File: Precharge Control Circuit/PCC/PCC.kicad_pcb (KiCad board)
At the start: 2 copper layers, 190.6 x 151.7 mm, 128 parts, among them J1 Conn_01x04_Socket, J10 AMP BYP, J11 AMP BYP, J2 874271202, J3 462070206, J4 Conn_02x14_Counter_Clockwise, J5 IMD, J6 Thermistor Expansion, J7 RTM, J8 BMS, J9 EnergyMeter, K1 Relay_SPDT, K2 PCN-112D3MHZ_000, Q1 IRLZ44N, Q2 IRLZ44N, U1 SN65HVD230, U2 4N35, U3 4N35, U7 TLV2372IP, U8 LM1117T-5.0

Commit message: Fixed Copper Zones on Resistor Divider, Fixed Mounting Holes and Placement, adjusted traces
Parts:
- added H1: MountingHole_Pad, MountingHole:MountingHole_3.2mm_M3_DIN965_Pad_TopBottom, F.Cu at (233.5, 21.2)
- added H2: MountingHole_Pad, MountingHole:MountingHole_3.2mm_M3_DIN965_Pad_TopBottom, F.Cu at (233.5, 158.8)
- added H3: MountingHole_Pad, MountingHole:MountingHole_3.2mm_M3_DIN965_Pad_TopBottom, F.Cu at (57.0, 20.7)
- added H4: MountingHole_Pad, MountingHole:MountingHole_3.2mm_M3_DIN965_Pad_TopBottom, F.Cu at (77.4, 160.5)
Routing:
- net +12 ISO: track 117.7 -> 123.5 mm, vias 8 -> 10
- net B+_in: track 124.4 -> 122.6 mm
- net /FusedTS+4: track 8.54 -> 6.90 mm
- net /FusedTS-2: track 15.9 -> 14.6 mm
- net /FusedTS+1: track 10.1 -> 8.96 mm
- net Net-(F5-Pad2): track 16.3 -> 15.5 mm
- net TS-: track 174.0 -> 173.4 mm
- added copper zone on B.Cu, net Net-(R1-Pad2)
- added copper zone on B.Cu, net Net-(R2-Pad2)
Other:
- outline, holes or cut-outs redrawn

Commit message: Acid Traps
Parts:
- moved R57 8.51 mm to (155.1, 81.2), turned to 180 degrees
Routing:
- net TS+: track 294.6 -> 308.9 mm
- net GLV+: track 256.7 -> 267.1 mm
- net Net-(R57-Pad2): track 11.4 -> 2.92 mm
- net GND ISO: track 42.9 -> 44.9 mm, vias 0 -> 1
- net Net-(F11-Pad2): track 16.6 -> 15.4 mm
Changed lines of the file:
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@@
 	(footprint "Resistor_SMD:R_0805_2012Metric"
 		(layer "B.Cu")
-		(at 159.004 73.66 -90)
+		(at 155.0875 81.21525 180)
 		(descr "Resistor SMD 0805 (2012 Metric), square (rectangular) end terminal, IPC-7351 nominal, (Body size source: IPC-SM-782 page 72, https://www.pcb-3d.com/wordpress/wp-content/uploads/ipc-sm-782a_amendment_1_and_2.pdf), generated with kicad-footprint-generator")
 		(tags "resistor")
 		(property "Reference" "R57"
-			(at 0 1.65 90)
+			(at 0 1.65 0)
 			(layer "B.SilkS")
 			(effects
@@
 		)
 		(property "Value" "510K"
-			(at 0 -1.65 90)
+			(at 0 -1.65 0)
 			(layer "B.Fab")
 			(effects
@@
 		)
 		(property "Datasheet" "https://www.digikey.com/en/products/detail/panasonic-electronic-components/ERJ-6GEYJ514V/83144"
-			(at 0 0 90)
+			(at 0 0 0)
 			(layer "B.Fab")
 			(hide yes)
@@
 		)
 		(property "Description" "Resistor, US symbol"
-			(at 0 0 90)
+			(at 0 0 0)
 			(layer "B.Fab")
 			(hide yes)
@@
 		)
 		(property "MFG" "Panasonic Electronic Components "
-			(at 0 0 270)
+			(at 0 0 180)
 			(unlocked yes)
 			(layer "B.Fab")
@@
 		)
 		(property "MPN" "ERJ-6GEYJ514V "
-			(at 0 0 270)
+			(at 0 0 180)
 			(unlocked yes)
 			(layer "B.Fab")
@@
 		)
 		(fp_text user "${REFERENCE}"
-			(at 0 0 90)
+			(at 0 0 0)
 			(layer "B.Fab")
 			(effects
@@
 		)
 		(pad "1" smd roundrect
-			(at -0.9125 0 270)
+			(at -0.9125 0 180)
 			(size 1.025 1.4)
 			(layers "B.Cu" "B.Mask" "B.Paste")
@@
 		)
 		(pad "2" smd roundrect
-			(at 0.9125 0 270)
+			(at 0.9125 0 180)
 			(size 1.025 1.4)
 			(layers "B.Cu" "B.Mask" "B.Paste")
@@
 		(net 7)
 	)
+	(via
+		(at 123.698 67.818)
+		(size 0.6)
+		(drill 0.3)
+		(layers "F.Cu" "B.Cu")
+		(net 8)
+	)
+	(segment
+		(start 124.559288 81.21525)
+		(end 124.302269 81.472269)
+		(width 0.7)
+		(layer "B.Cu")
+		(net 8)
+	)
 	(segment
 		(start 122.425 83.37675)
@@
 	)
 	(segment
-		(start 124.559288 81.21525)
+		(start 124.302269 81.472269)
 		(end 122.425 83.349538)
 		(width 0.7)
@@
 	)
 	(segment
+		(start 124.302269 80.304981)
+		(end 123.698 79.700712)
+		(width 0.7)
+		(layer "B.Cu")
+		(net 8)
+	)
+	(segment
 		(start 148.475 28.59)
 		(end 133.41 28.59)
@@
 	)
 	(segment
+		(start 124.302269 81.472269)
+		(end 124.302269 80.304981)
+		(width 0.7)
+		(layer "B.Cu")
+		(net 8)
+	)
+	(segment
 		(start 132.4635 81.21525)
 		(end 125.212538 81.21525)
@@
 	)
 	(segment
-		(start 158.75 71.882)
-		(end 158.75 62.75)
+		(start 167.879 71.879)
+		(end 171.876995 71.879)
 		(width 2)
 		(layer "B.Cu")
@@
 	)
 	(segment
+		(start 156 65.5)
+		(end 158.75 62.75)
+		(width 0.5)
+		(layer "B.Cu")
+		(net 41)
+	)
+	(segment
 		(start 200.475747 164.259253)
 		(end 213.36 151.375)
@@
 	)
 	(segment
-		(start 171.873995 71.882)
-		(end 158.75 71.882)
-		(width 2)
-		(layer "B.Cu")
-		(net 41)
-	)
-	(segment
 		(start 213.36 75.955)
 		(end 209.287 71.882)
@@
 	)
 	(segment
+		(start 156 81.21525)
+		(end 156 65.5)
+		(width 0.5)
+		(layer "B.Cu")
+		(net 41)
+	)
+	(segment
+		(start 158.75 62.75)
+		(end 167.879 71.879)
+		(width 2)
+		(layer "B.Cu")
+		(net 41)
+	)
+	(segment
 		(start 111.25 145.2125)
 		(end 115.5375 149.5)
@@
 	)
 	(segment
-		(start 61.45 124.79)
+		(start 63.87 124.79)
 		(end 65.000502 124.79)
 		(width 2)
@@
 	)
 	(segment
+		(start 64.253304 85.346699)
+		(end 67.44 85.346699)
+		(width 2)
+		(layer "B.Cu")
+		(net 48)
+	)
+	(segment
 		(start 68.901 128.690498)
 		(end 68.901 134.189)
@@
 	)
 	(segment
-		(start 68.901 134.189)
+		(start 61.45 124.79)
+		(end 63.87 124.79)
+		(width 2)
+		(layer "B.Cu")
+		(net 48)
+	)
+	(segment
+		(start 66.355 136.735)
 		(end 64.55 138.54)
 		(width 2)
@@
 	)
 	(segment
+		(start 67.44 85.346699)
+		(end 67.44 82.160004)
+		(width 2)
+		(layer "B.Cu")
+		(net 48)
+	)
+	(segment
+		(start 65.905251 139.694749)
+		(end 65.905251 137.184749)
+		(width 2)
+		(layer "B.Cu")
+		(net 48)
+	)
+	(segment
+		(start 68.901 134.189)
+		(end 66.355 136.735)
+		(width 2)
+		(layer "B.Cu")
+		(net 48)
+	)
+	(segment
+		(start 66.155251 139.944749)
+		(end 65.905251 139.694749)
+		(width 2)
+		(layer "B.Cu")
+		(net 48)
+	)
+	(segment
 		(start 60.399 102.04205)
 		(end 60.399 109.489)
@@
 	)
 	(segment
-		(start 64.253304 85.346699)
+		(start 67.44 82.160004)
+		(end 67.820002 81.780002)
+		(width 2)
+		(layer "B.Cu")
+		(net 48)
+	)
+	(segment
+		(start 67.44 85.346699)
 		(end 71.344183 85.346699)
 		(width 2)
@@
 	)
 	(segment
+		(start 64.38 121.86)
+		(end 61.45 124.79)
+		(width 2)
+		(layer "B.Cu")
+		(net 48)
+	)
+	(segment
+		(start 67.820002 81.780002)
+		(end 61.300001 88.300002)
+		(width 2)
+		(layer "B.Cu")
+		(net 48)
+	)
+	(segment
 		(start 71.344183 85.346699)
 		(end 72.962301 86.964817)
@@
 	)
 	(segment
+		(start 65.905251 137.184749)
+		(end 66.355 136.735)
+		(width 2)
+		(layer "B.Cu")
+		(net 48)
+	)
+	(segment
 		(start 61.300001 74.300002)
 		(end 64.253304 71.346699)
@@
 	)
 	(segment
+		(start 63.87 122.37)
+		(end 64.38 121.86)
+		(width 2)
+		(layer "B.Cu")
+		(net 48)
+	)
+	(segment
 		(start 68.901 114.440498)
 		(end 68.901 117.339)
@@
 	(segment
 		(start 68.901 117.339)
-		(end 61.45 124.79)
+		(end 64.38 121.86)
 		(width 2)
 		(layer "B.Cu")
@@
 	)
 	(segment
-		(start 64.750502 138.54)
+		(start 66.155251 139.944749)
 		(end 68.651 142.440498)
 		(width 2)
@@
 	)
 	(segment
+		(start 64.750502 138.54)
+		(end 66.155251 139.944749)
+		(width 2)
+		(layer "B.Cu")
+		(net 48)
+	)
+	(segment
 		(start 72.962301 86.964817)
 		(end 72.962301 89.478749)
@@
 	)
 	(segment
+		(start 63.87 124.79)
+		(end 63.87 122.37)
+		(width 2)
+		(layer "B.Cu")
+		(net 48)
+	)
+	(segment
 		(start 72.962301 89.478749)
 		(end 60.399 102.04205)
@@
 	(segment
 		(start 72.962301 76.637702)
-		(end 61.300001 88.300002)
+		(end 67.820002 81.780002)
 		(width 2)
 		(layer "B.Cu")
@@
 	)
 	(segment
-		(start 154.49675 81.21525)
-		(end 159.004 76.708)
-		(width 0.2)
-		(layer "B.Cu")
-		(net 83)
-	)
-	(segment
-		(start 159.004 76.708)
-		(end 159.004 74.5725)
-		(width 0.2)
-		(layer "B.Cu")
-		(net 83)
-	)
-	(segment
 		(start 102.445 44.25)
 		(end 101.195253 43.000253)
@@
 	)
 	(segment
-		(start 197.9515 100.33)
-		(end 199.7295 102.108)
-		(width 0.7)
-		(layer "B.Cu")
-		(net 109)
-	)
-	(segment
-		(start 189.475 100.33)
-		(end 197.9515 100.33)
+		(start 201.3965 102.108)
+		(end 191.253 102.108)
 		(width 0.7)
 		(layer "B.Cu")
@@
 	)
 	(segment
-		(start 199.7295 102.108)
-		(end 201.3965 102.108)
+		(start 191.253 102.108)
+		(end 189.475 100.33)
 		(width 0.7)
 		(layer "B.Cu")
@@
 	)
 	(segment
-		(start 195.624 88.265)
-		(end 198.037 85.852)
+		(start 193.158 85.852)
+		(end 190.745 88.265)
 		(width 0.7)
 		(layer "B.Cu")
@@
 	)
 	(segment
-		(start 198.037 85.852)
-		(end 199.4915 85.852)
+		(start 199.4915 85.852)
+		(end 193.158 85.852)
 		(width 0.7)
 		(layer "B.Cu")
@@
 	)
 	(segment
-		(start 190.745 88.265)
-		(end 195.624 88.265)
-		(width 0.7)
-		(layer "B.Cu")
-		(net 110)
-	)
-	(segment
-		(start 230.759 108.0515)
-		(end 230.759 106.724)
-		(width 0.7)
-		(layer "B.Cu")
-		(net 111)
-	)
-	(segment
-		(start 230.759 106.724)
-		(end 229.235 105.2)
-		(width 0.7)
-		(layer "B.Cu")
-		(net 111)
-	)
-	(segment
-		(start 229.235 105.2)
+		(start 230.759 94.479)
 		(end 229.235 92.955)
 		(width 0.7)
@@
 	)
 	(segment
-		(start 213.36 92.955)
-		(end 220.546 92.955)
+		(start 230.759 108.0515)
+		(end 230.759 94.479)
 		(width 0.7)
 		(layer "B.Cu")
-		(net 112)
+		(net 111)
 	)
 	(segment
-		(start 220.546 92.955)
-		(end 225.806 98.215)
+		(start 220.5825 100.1775)
+		(end 213.36 92.955)
 		(width 0.7)
 		(layer "B.Cu")
@@
 	)
 	(segment
-		(start 225.806 98.215)
-		(end 225.806 100.1775)
+		(start 225.806 100.1775)
+		(end 220.5825 100.1775)
 		(width 0.7)
 		(layer "B.Cu")

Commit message: PCC rev added port
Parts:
- added J12: INVTR, Connector_Molex:Molex_Mini-Fit_Jr_5566-04A2_2x02_P4.20mm_Vertical, F.Cu at (57.6, 154.0)
- moved J7 84.3 mm to (82.8, 73.3), turned to -90 degrees
- moved C6 1.37 mm to (87.1, 78.8)
- moved Q2 0.86 mm to (75.7, 104.3)
- moved R30 0.86 mm to (89.4, 78.7)
- moved Q1 0.80 mm to (87.0, 104.3)
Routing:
- net RTM_SIG: track 85.0 -> 38.1 mm, vias 0 -> 1
- net GLV+: track 267.1 -> 296.9 mm
- net CANL: track 113.5 -> 129.3 mm
- net CANH: track 104.1 -> 119.9 mm
- net PreDis_IR-: track 42.6 -> 51.2 mm
- net IR+ CTRL: track 52.4 -> 56.2 mm
- net IR-_GND: track 59.1 -> 57.5 mm
- net IR+_GND: track 24.4 -> 25.3 mm
- net /NTC 2: track 49.4 -> 48.6 mm
- net GLV-: vias 131 -> 216
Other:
- board text added: "12v"
- board text added: "DNP"
- board text added: "INVERTER"
- board text added: "THRMSTR"
- board text added: "sig"
- board text removed: "RTML (ONLY!)"
- board text removed: "THERMISTOR"

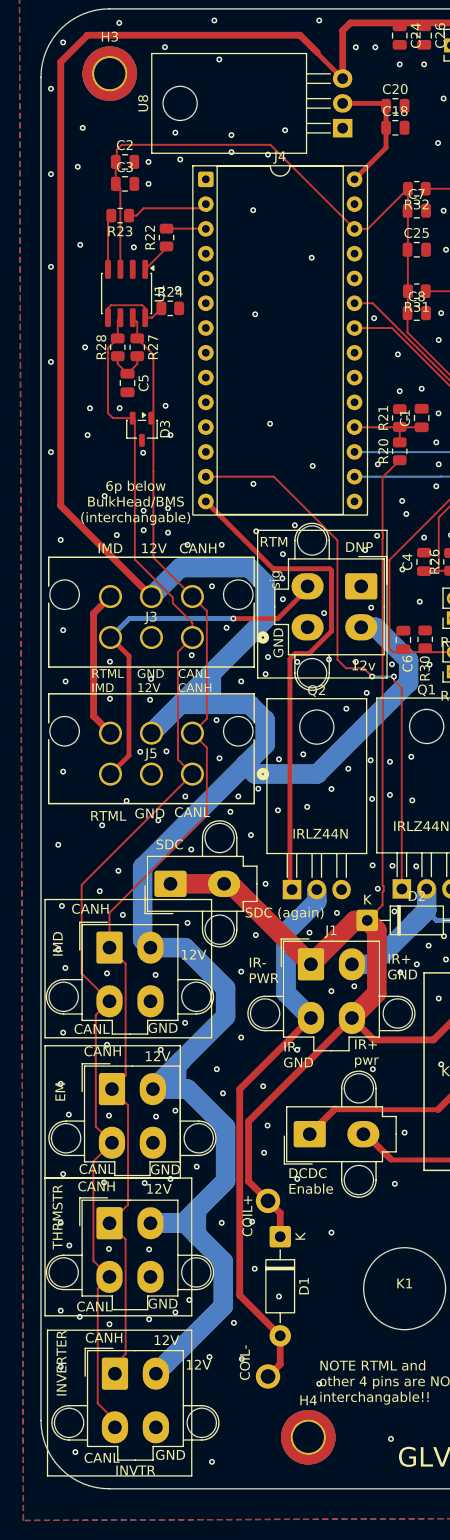
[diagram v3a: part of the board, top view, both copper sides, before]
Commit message: moved around connectors
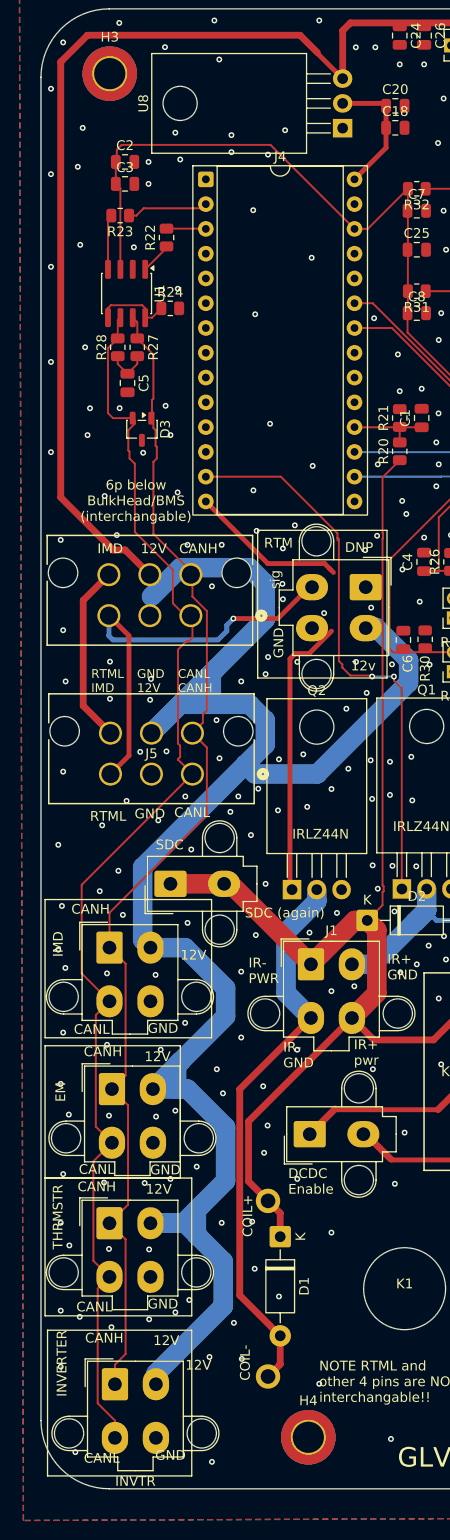
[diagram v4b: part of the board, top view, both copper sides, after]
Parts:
- moved J3 2.25 mm to (65.3, 76.3)
- moved J12 1.08 mm to (57.6, 155.0)
- moved J7 0.46 mm to (83.3, 73.3)
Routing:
- net PreDis_IR-: track 51.2 -> 45.3 mm
- net RTM_SIG: track 38.1 -> 43.3 mm
- net IMD_Fault: track 15.4 -> 18.5 mm
- net CANL: track 129.3 -> 132.1 mm
- net CANH: track 119.9 -> 122.1 mm
- net IR+ CTRL: track 56.2 -> 57.1 mm
- net GLV+: track 296.9 -> 296.3 mm
- net GLV-: vias 216 -> 210

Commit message: updates I think
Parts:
- K2: value PCN-112D3MHZ_000 -> PCN-105D3MHZ,000
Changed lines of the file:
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@@
 			)
 		)
-		(property "Value" "PCN-112D3MHZ_000"
+		(property "Value" "PCN-105D3MHZ,000"
 			(at -1.27 8.7249 0)
 			(unlocked yes)
@@
 			)
 		)
-		(property "MPN" "PCN-112D3MHZ,000 "
+		(property "MPN" "PCN-105D3MHZ,000"
 			(at 0 0 0)
 			(unlocked yes)

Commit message: silkscreen, last touches time to order
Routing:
- net PreDis_IR-: track 45.3 -> 51.7 mm
- net GLV+: track 296.3 -> 299.1 mm

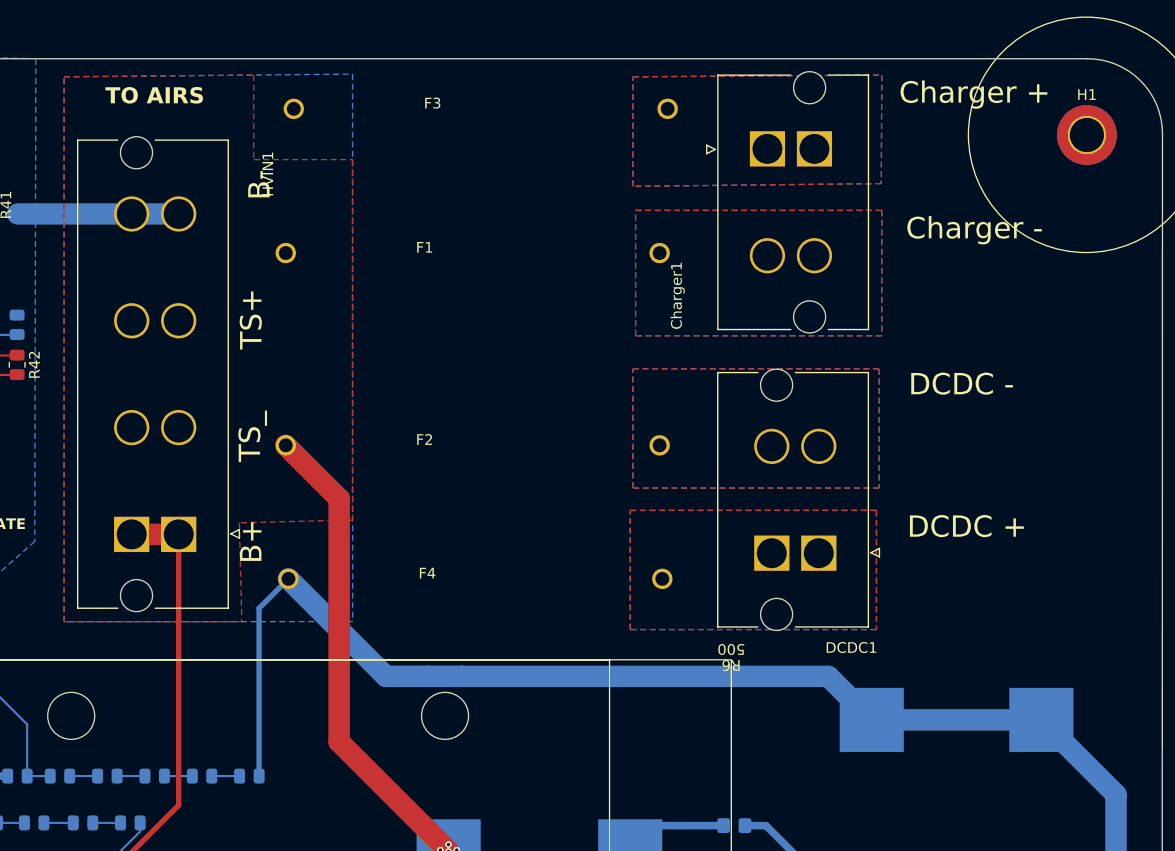
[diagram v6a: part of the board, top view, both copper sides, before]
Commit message: fuse holders added
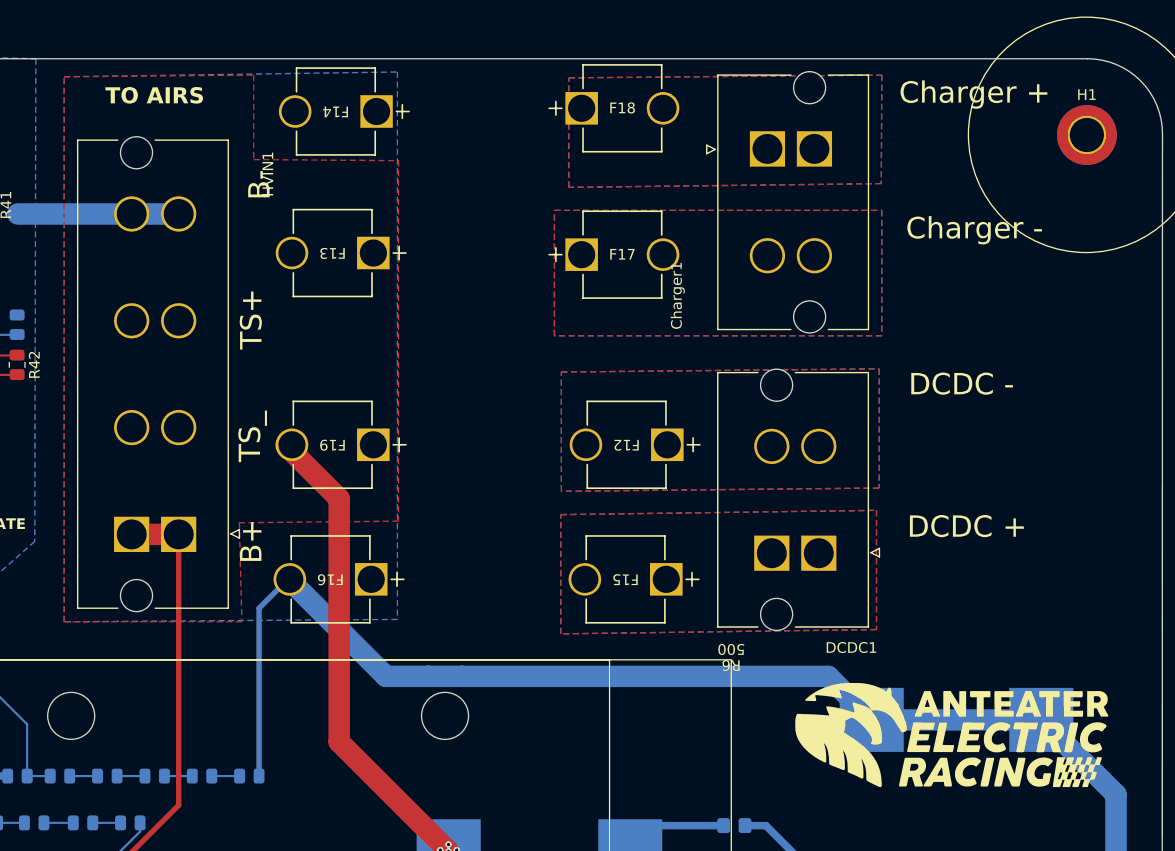
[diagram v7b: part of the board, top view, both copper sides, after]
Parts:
- removed F1, F2, F3, F4: 20A, footprints:ЗAВ 33x7mm fuse(axial lead)
- added F12: 01220088Z, footprints:FuseHolder, F.Cu at (194.2, 50.2)
- added F13: 01220088Z, footprints:FuseHolder, F.Cu at (166.7, 32.2)
- added F14: 01220088Z, footprints:FuseHolder, F.Cu at (167.0, 19.0)
- added F15: 01220088Z, footprints:FuseHolder, F.Cu at (194.1, 62.8)
- added F16: 01220088Z, footprints:FuseHolder, F.Cu at (166.5, 62.8)
- added F17: 01220088Z, footprints:FuseHolder, F.Cu at (186.2, 32.4)
- added F18: 01220088Z, footprints:FuseHolder, F.Cu at (186.2, 18.7)
- added F19: 01220088Z, footprints:FuseHolder, F.Cu at (166.7, 50.2)
- K2: value PCN-105D3MHZ,000 -> PCN-112D3MHZ_000
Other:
- board text added: "Precharge Control Circuit Originally By Bill Yuan Updated by Gabriel Schoene"
